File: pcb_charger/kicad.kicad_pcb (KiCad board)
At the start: 2 copper layers, 100 x 30 mm, 12 parts, among them J1 B+, J2 B-, J3 OUT+, J4 OUT-, M1 TP4056Module, SW1 SW_SPDT

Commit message: All 3 parts done
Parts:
- moved J4 0.70 mm to (80.6, 23.0)
- moved J3 0.50 mm to (60.5, 23.0)
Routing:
- net Net-(J3-Pad1): track 41.6 -> 38.9 mm
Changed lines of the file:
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@@
     (thickness 1.6)
     (drawings 91)
-    (tracks 35)
+    (tracks 33)
     (zones 0)
     (modules 12)
@@
     (mod_text_size 1 1)
     (mod_text_width 0.15)
-    (pad_size 15 2.5)
+    (pad_size 15 3)
     (pad_drill 0)
     (pad_to_mask_clearance 0.2)
@@
   )
   (module Connector_Wire:SolderWirePad_1x01_Drill0.8mm (layer B.Cu)
-    (at 80.575 22.3)
+    (at 80.575 23)
     (descr "Wire solder connection")
     (tags connector)
@@
       (effects (font (size 1 1) (thickness 0.15)) (justify mirror))
     )
-    (pad 1 smd oval (at 0 0) (size 15 2.5) (layers B.Cu B.Paste B.Mask)
+    (pad 1 smd oval (at 0 0) (size 15 3) (layers B.Cu B.Paste B.Mask)
       (net 4 "Net-(J4-Pad1)"))
   )
   (module Connector_Wire:SolderWirePad_1x01_Drill0.8mm (layer B.Cu)
-    (at 60.5 22.5)
+    (at 60.5 23)
     (descr "Wire solder connection")
     (tags connector)
@@
       (effects (font (size 1 1) (thickness 0.15)) (justify mirror))
     )
-    (pad 1 smd oval (at 0 0) (size 15 2.5) (layers B.Cu B.Paste B.Mask)
+    (pad 1 smd oval (at 0 0) (size 15 3) (layers B.Cu B.Paste B.Mask)
       (net 3 "Net-(J3-Pad1)"))
   )
@@
   (segment (start 84.25 44.118) (end 84.216 44.084) (width 0.3) (layer F.Cu) (net 3))
   (segment (start 84.25 47.07) (end 84.25 44.118) (width 0.3) (layer F.Cu) (net 3))
-  (segment (start 84.216 44.084) (end 84.216 33.924) (width 0.3) (layer B.Cu) (net 3))
-  (segment (start 84.216 33.924) (end 75.072 24.78) (width 0.3) (layer B.Cu) (net 3))
-  (segment (start 68.3 22.5) (end 60.5 22.5) (width 0.3) (layer B.Cu) (net 3))
-  (segment (start 70.58 24.78) (end 68.3 22.5) (width 0.3) (layer B.Cu) (net 3))
-  (segment (start 75.072 24.78) (end 70.58 24.78) (width 0.3) (layer B.Cu) (net 3))
+  (segment (start 84.216 38.216) (end 84.216 44.084) (width 0.3) (layer B.Cu) (net 3))
+  (segment (start 60.5 23) (end 69 23) (width 0.3) (layer B.Cu) (net 3))
+  (segment (start 69 23) (end 84.216 38.216) (width 0.3) (layer B.Cu) (net 3))
   (segment (start 80.575 23.85) (end 80.575 22.3) (width 0.3) (layer B.Cu) (net 4))
   (segment (start 80.575 28.875) (end 80.575 28.075) (width 0.3) (layer B.Cu) (net 4))

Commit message: Last changes to the charger board and gerbers
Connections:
- net Net-(J1-Pad1) renamed /B+
- net Net-(J2-Pad1) renamed /B-
- net Net-(J3-Pad1) renamed /OUT+on
- net Net-(J4-Pad1) renamed /OUT-
- net Net-(M1-Pad5) renamed /OUT+
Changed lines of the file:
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@@
   )
   (net 0 "")
-  (net 1 "Net-(J1-Pad1)")
-  (net 2 "Net-(J2-Pad1)")
-  (net 3 "Net-(J3-Pad1)")
-  (net 4 "Net-(J4-Pad1)")
-  (net 5 "Net-(M1-Pad5)")
+  (net 1 /B+)
+  (net 2 /B-)
+  (net 3 /OUT+on)
+  (net 4 /OUT-)
+  (net 5 /OUT+)
   (net_class Default "This is the default net class."
     (clearance 0.2)
@@
     (uvia_dia 0.3)
     (uvia_drill 0.1)
-    (add_net "Net-(J1-Pad1)")
-    (add_net "Net-(J2-Pad1)")
-    (add_net "Net-(J3-Pad1)")
-    (add_net "Net-(J4-Pad1)")
-    (add_net "Net-(M1-Pad5)")
+    (add_net /B+)
+    (add_net /B-)
+    (add_net /OUT+)
+    (add_net /OUT+on)
+    (add_net /OUT-)
   )
   (module logos:roommonitor-rev (layer F.Cu)
@@
     (pad 3 smd rect (at 2.25 -1.43) (size 0.7 1.5) (layers F.Cu F.Paste F.Mask))
     (pad 2 smd rect (at 0.75 -1.43) (size 0.7 1.5) (layers F.Cu F.Paste F.Mask)
-      (net 5 "Net-(M1-Pad5)"))
+      (net 5 /OUT+))
     (pad 1 smd rect (at -2.25 -1.43) (size 0.7 1.5) (layers F.Cu F.Paste F.Mask)
-      (net 3 "Net-(J3-Pad1)"))
+      (net 3 /OUT+on))
     (pad "" np_thru_hole circle (at 1.5 0.33) (size 0.9 0.9) (drill 0.9) (layers *.Cu *.Mask))
     (pad "" np_thru_hole circle (at -1.5 0.33) (size 0.9 0.9) (drill 0.9) (layers *.Cu *.Mask))
@@
     (pad 2 smd rect (at -11 -6.75 180) (size 3 3) (layers B.Cu B.Paste B.Mask))
     (pad 6 smd rect (at 11 -7 180) (size 3 2.5) (layers B.Cu B.Paste B.Mask)
-      (net 4 "Net-(J4-Pad1)"))
+      (net 4 /OUT-))
     (pad 5 smd rect (at 11 7 180) (size 3 2.5) (layers B.Cu B.Paste B.Mask)
-      (net 5 "Net-(M1-Pad5)"))
+      (net 5 /OUT+))
     (pad 3 smd rect (at 11 3.75 180) (size 3 2.5) (layers B.Cu B.Paste B.Mask)
-      (net 1 "Net-(J1-Pad1)"))
+      (net 1 /B+))
     (pad 4 smd rect (at 11 -3.75 180) (size 3 2.5) (layers B.Cu B.Paste B.Mask)
-      (net 2 "Net-(J2-Pad1)"))
+      (net 2 /B-))
   )
   (module Connector_Wire:SolderWirePad_1x01_Drill0.8mm (layer B.Cu)
@@
     )
     (pad 1 smd oval (at 0 0) (size 15 3) (layers B.Cu B.Paste B.Mask)
-      (net 4 "Net-(J4-Pad1)"))
+      (net 4 /OUT-))
   )
   (module Connector_Wire:SolderWirePad_1x01_Drill0.8mm (layer B.Cu)
@@
     )
     (pad 1 smd oval (at 0 0) (size 15 3) (layers B.Cu B.Paste B.Mask)
-      (net 3 "Net-(J3-Pad1)"))
+      (net 3 /OUT+on))
   )
   (module Connector_Wire:SolderWirePad_1x01_Drill0.8mm (layer B.Cu)
@@
     )
     (pad 1 smd oval (at 0 0) (size 14 2.5) (layers B.Cu B.Paste B.Mask)
-      (net 2 "Net-(J2-Pad1)"))
+      (net 2 /B-))
   )
   (module Connector_Wire:SolderWirePad_1x01_Drill0.8mm (layer B.Cu)
@@
     )
     (pad 1 smd oval (at 0 0) (size 14 2.5) (layers B.Cu B.Paste B.Mask)
-      (net 1 "Net-(J1-Pad1)"))
+      (net 1 /B+))
   )
   (gr_text OFF (at 93 49) (layer F.SilkS)
@@
   (via (at 92.598 32.908) (size 0.6) (drill 0.4) (layers F.Cu B.Cu) (net 1))
   (segment (start 51.378 24.2) (end 51.45 24.272) (width 0.3) (layer B.Cu) (net 1))
-  (segment (start 42.9 24.2) (end 51.378 24.2) (width 0.3) (layer B.Cu) (net 1))
+  (segment (start 42.9 24.2) (end 51.378 24.2) (width 0.3) (layer B.Cu) (net 1) (status 10))
   (segment (start 92.994001 32.511999) (end 92.598 32.908) (width 0.3) (layer F.Cu) (net 1))
   (segment (start 92.994001 29.547999) (end 92.994001 32.511999) (width 0.3) (layer F.Cu) (net 1))
-  (segment (start 51.45 24.272) (end 87.718002 24.272) (width 0.3) (layer F.Cu) (net 1))
   (segment (start 87.718002 24.272) (end 92.994001 29.547999) (width 0.3) (layer F.Cu) (net 1))
   (segment (start 93.756 31.75) (end 92.598 32.908) (width 0.3) (layer B.Cu) (net 1))
-  (segment (start 96 31.75) (end 93.756 31.75) (width 0.3) (layer B.Cu) (net 1))
+  (segment (start 96 31.75) (end 93.756 31.75) (width 0.3) (layer B.Cu) (net 1) (status 10))
+  (segment (start 51.45 24.272) (end 87.718002 24.272) (width 0.3) (layer F.Cu) (net 1))
   (segment (start 97.85 25.7) (end 102 29.85) (width 0.3) (layer B.Cu) (net 2))
-  (segment (start 97.85 24.15) (end 97.85 25.7) (width 0.3) (layer B.Cu) (net 2))
+  (segment (start 97.85 24.15) (end 97.85 25.7) (width 0.3) (layer B.Cu) (net 2) (status 10))
   (segment (start 102 29.85) (end 102 36) (width 0.3) (layer B.Cu) (net 2))
-  (segment (start 98.75 39.25) (end 96 39.25) (width 0.3) (layer B.Cu) (net 2))
+  (segment (start 98.75 39.25) (end 96 39.25) (width 0.3) (layer B.Cu) (net 2) (status 20))
   (segment (start 102 36) (end 98.75 39.25) (width 0.3) (layer B.Cu) (net 2))
   (via (at 84.216 44.084) (size 0.6) (drill 0.4) (layers F.Cu B.Cu) (net 3))
   (segment (start 84.25 44.118) (end 84.216 44.084) (width 0.3) (layer F.Cu) (net 3))
-  (segment (start 84.25 47.07) (end 84.25 44.118) (width 0.3) (layer F.Cu) (net 3))
+  (segment (start 84.25 47.07) (end 84.25 44.118) (width 0.3) (layer F.Cu) (net 3) (status 10))
   (segment (start 84.216 38.216) (end 84.216 44.084) (width 0.3) (layer B.Cu) (net 3))
-  (segment (start 60.5 23) (end 69 23) (width 0.3) (layer B.Cu) (net 3))
+  (segment (start 60.5 23) (end 69 23) (width 0.3) (layer B.Cu) (net 3) (status 10))
   (segment (start 69 23) (end 84.216 38.216) (width 0.3) (layer B.Cu) (net 3))
-  (segment (start 80.575 23.85) (end 80.575 22.3) (width 0.3) (layer B.Cu) (net 4))
+  (segment (start 80.575 23.85) (end 80.575 22.3) (width 0.3) (layer B.Cu) (net 4) (status 30))
   (segment (start 80.575 28.875) (end 80.575 28.075) (width 0.3) (layer B.Cu) (net 4))
   (segment (start 94.2 42.5) (end 80.575 28.875) (width 0.3) (layer B.Cu) (net 4))
-  (segment (start 96 42.5) (end 94.2 42.5) (width 0.3) (layer B.Cu) (net 4))
+  (segment (start 96 42.5) (end 94.2 42.5) (width 0.3) (layer B.Cu) (net 4) (status 10))
   (segment (start 80.575 28.825) (end 80.575 28.075) (width 0.3) (layer B.Cu) (net 4))
-  (segment (start 80.575 28.075) (end 80.575 23.85) (width 0.3) (layer B.Cu) (net 4))
+  (segment (start 80.575 28.075) (end 80.575 23.85) (width 0.3) (layer B.Cu) (net 4) (status 20))
   (via (at 92.344 29.86) (size 0.6) (drill 0.4) (layers F.Cu B.Cu) (net 5))
   (segment (start 92.484 30) (end 92.344 29.86) (width 0.3) (layer B.Cu) (net 5))
-  (segment (start 87.25 34.954) (end 87.25 47.07) (width 0.3) (layer F.Cu) (net 5))
+  (segment (start 87.25 34.954) (end 87.25 47.07) (width 0.3) (layer F.Cu) (net 5) (status 20))
   (segment (start 92.344 29.86) (end 87.25 34.954) (width 0.3) (layer F.Cu) (net 5))
   (segment (start 93.704 28.5) (end 92.344 29.86) (width 0.3) (layer B.Cu) (net 5))
-  (segment (start 96 28.5) (end 93.704 28.5) (width 0.3) (layer B.Cu) (net 5))
+  (segment (start 96 28.5) (end 93.704 28.5) (width 0.3) (layer B.Cu) (net 5) (status 10))
 )

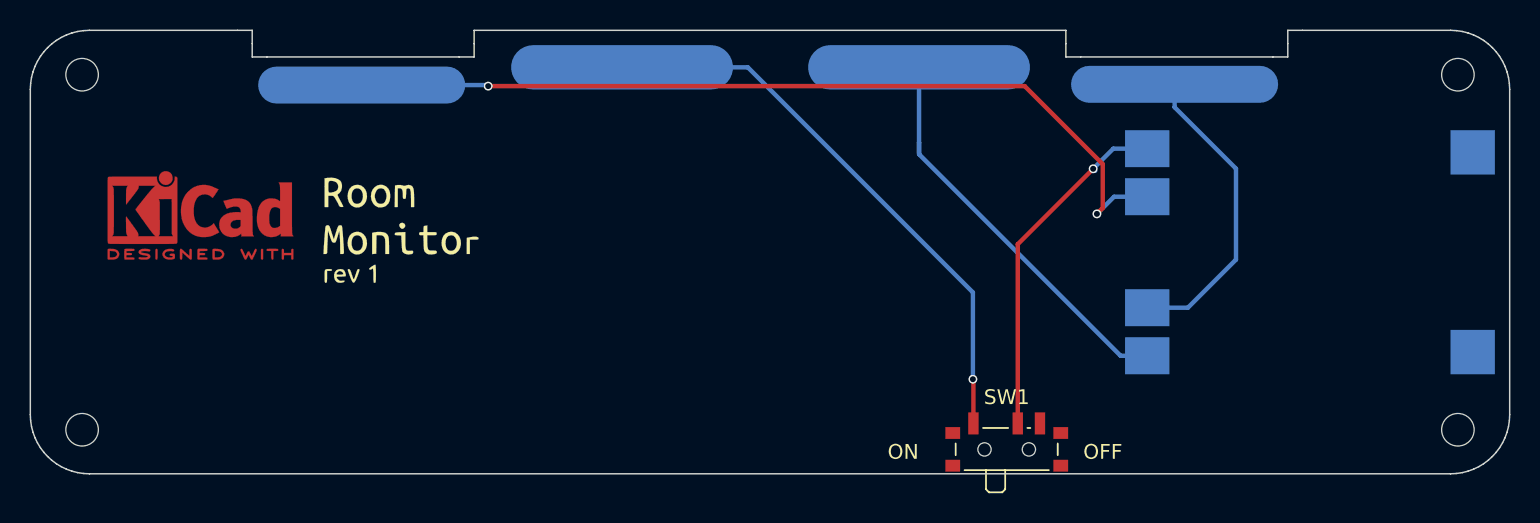
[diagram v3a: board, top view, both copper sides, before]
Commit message: Update trace and via sizes for battery and charger
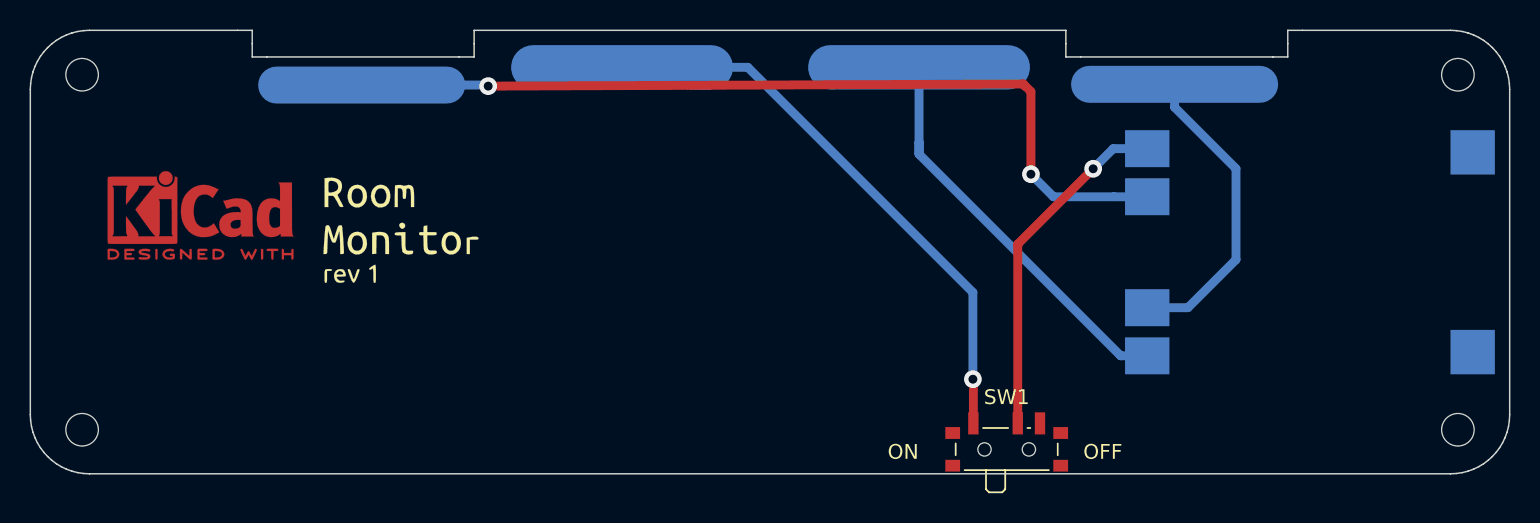
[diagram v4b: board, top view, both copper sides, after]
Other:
- net class Battery added: clearance 0.4, trace_width 0.6, via_dia 1.2, via_drill 0.6
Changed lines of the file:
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@@
-(kicad_pcb (version 20171130) (host pcbnew 5.1.4-e60b266~84~ubuntu19.04.1)
+(kicad_pcb (version 20171130) (host pcbnew 5.1.5-52549c5~84~ubuntu19.04.1)
   (general
     (thickness 1.6)
     (drawings 91)
-    (tracks 33)
+    (tracks 36)
     (zones 0)
     (modules 12)
@@
     (via_dia 0.6)
     (via_drill 0.4)
+    (uvia_dia 0.3)
+    (uvia_drill 0.1)
+  )
+  (net_class Battery ""
+    (clearance 0.4)
+    (trace_width 0.6)
+    (via_dia 1.2)
+    (via_drill 0.6)
     (uvia_dia 0.3)
     (uvia_drill 0.1)
@@
   (gr_line (start 116.499999 50.477394) (end 116.499999 50.477394) (layer Edge.Cuts) (width 0.1))
   (gr_line (start 116.499999 50.477394) (end 116.499999 50.477394) (layer Edge.Cuts) (width 0.1))
-  (via (at 51.45 24.272) (size 0.6) (drill 0.4) (layers F.Cu B.Cu) (net 1))
-  (via (at 92.598 32.908) (size 0.6) (drill 0.4) (layers F.Cu B.Cu) (net 1))
-  (segment (start 51.378 24.2) (end 51.45 24.272) (width 0.3) (layer B.Cu) (net 1))
-  (segment (start 42.9 24.2) (end 51.378 24.2) (width 0.3) (layer B.Cu) (net 1) (status 10))
-  (segment (start 92.994001 32.511999) (end 92.598 32.908) (width 0.3) (layer F.Cu) (net 1))
-  (segment (start 92.994001 29.547999) (end 92.994001 32.511999) (width 0.3) (layer F.Cu) (net 1))
-  (segment (start 87.718002 24.272) (end 92.994001 29.547999) (width 0.3) (layer F.Cu) (net 1))
-  (segment (start 93.756 31.75) (end 92.598 32.908) (width 0.3) (layer B.Cu) (net 1))
-  (segment (start 96 31.75) (end 93.756 31.75) (width 0.3) (layer B.Cu) (net 1) (status 10))
-  (segment (start 51.45 24.272) (end 87.718002 24.272) (width 0.3) (layer F.Cu) (net 1))
-  (segment (start 97.85 25.7) (end 102 29.85) (width 0.3) (layer B.Cu) (net 2))
-  (segment (start 97.85 24.15) (end 97.85 25.7) (width 0.3) (layer B.Cu) (net 2) (status 10))
-  (segment (start 102 29.85) (end 102 36) (width 0.3) (layer B.Cu) (net 2))
-  (segment (start 98.75 39.25) (end 96 39.25) (width 0.3) (layer B.Cu) (net 2) (status 20))
-  (segment (start 102 36) (end 98.75 39.25) (width 0.3) (layer B.Cu) (net 2))
-  (via (at 84.216 44.084) (size 0.6) (drill 0.4) (layers F.Cu B.Cu) (net 3))
-  (segment (start 84.25 44.118) (end 84.216 44.084) (width 0.3) (layer F.Cu) (net 3))
-  (segment (start 84.25 47.07) (end 84.25 44.118) (width 0.3) (layer F.Cu) (net 3) (status 10))
-  (segment (start 84.216 38.216) (end 84.216 44.084) (width 0.3) (layer B.Cu) (net 3))
-  (segment (start 60.5 23) (end 69 23) (width 0.3) (layer B.Cu) (net 3) (status 10))
-  (segment (start 69 23) (end 84.216 38.216) (width 0.3) (layer B.Cu) (net 3))
-  (segment (start 80.575 23.85) (end 80.575 22.3) (width 0.3) (layer B.Cu) (net 4) (status 30))
-  (segment (start 80.575 28.875) (end 80.575 28.075) (width 0.3) (layer B.Cu) (net 4))
-  (segment (start 94.2 42.5) (end 80.575 28.875) (width 0.3) (layer B.Cu) (net 4))
-  (segment (start 96 42.5) (end 94.2 42.5) (width 0.3) (layer B.Cu) (net 4) (status 10))
-  (segment (start 80.575 28.825) (end 80.575 28.075) (width 0.3) (layer B.Cu) (net 4))
-  (segment (start 80.575 28.075) (end 80.575 23.85) (width 0.3) (layer B.Cu) (net 4) (status 20))
-  (via (at 92.344 29.86) (size 0.6) (drill 0.4) (layers F.Cu B.Cu) (net 5))
-  (segment (start 92.484 30) (end 92.344 29.86) (width 0.3) (layer B.Cu) (net 5))
-  (segment (start 87.25 34.954) (end 87.25 47.07) (width 0.3) (layer F.Cu) (net 5) (status 20))
-  (segment (start 92.344 29.86) (end 87.25 34.954) (width 0.3) (layer F.Cu) (net 5))
-  (segment (start 93.704 28.5) (end 92.344 29.86) (width 0.3) (layer B.Cu) (net 5))
-  (segment (start 96 28.5) (end 93.704 28.5) (width 0.3) (layer B.Cu) (net 5) (status 10))
+  (via (at 51.45 24.272) (size 1.2) (drill 0.6) (layers F.Cu B.Cu) (net 1))
+  (segment (start 51.378 24.2) (end 51.45 24.272) (width 0.6) (layer B.Cu) (net 1))
+  (segment (start 42.9 24.2) (end 51.378 24.2) (width 0.6) (layer B.Cu) (net 1) (status 10))
+  (segment (start 96 31.75) (end 93.756 31.75) (width 0.6) (layer B.Cu) (net 1) (status 10))
+  (segment (start 93.756 31.75) (end 89.662 31.75) (width 0.6) (layer B.Cu) (net 1))
+  (segment (start 89.662 31.75) (end 88.138 30.226) (width 0.6) (layer B.Cu) (net 1))
+  (segment (start 88.138 30.226) (end 88.138 30.226) (width 0.6) (layer B.Cu) (net 1))
+  (via (at 88.138 30.226) (size 1.2) (drill 0.6) (layers F.Cu B.Cu) (net 1))
+  (segment (start 88.138 24.638) (end 87.63 24.13) (width 0.6) (layer F.Cu) (net 1))
+  (segment (start 88.138 30.226) (end 88.138 24.638) (width 0.6) (layer F.Cu) (net 1))
+  (segment (start 51.45 24.272) (end 87.63 24.13) (width 0.6) (layer F.Cu) (net 1))
+  (segment (start 87.63 24.13) (end 87.718002 24.272) (width 0.6) (layer F.Cu) (net 1))
+  (segment (start 97.85 25.7) (end 102 29.85) (width 0.6) (layer B.Cu) (net 2))
+  (segment (start 97.85 24.15) (end 97.85 25.7) (width 0.6) (layer B.Cu) (net 2) (status 10))
+  (segment (start 102 29.85) (end 102 36) (width 0.6) (layer B.Cu) (net 2))
+  (segment (start 98.75 39.25) (end 96 39.25) (width 0.6) (layer B.Cu) (net 2) (status 20))
+  (segment (start 102 36) (end 98.75 39.25) (width 0.6) (layer B.Cu) (net 2))
+  (via (at 84.216 44.084) (size 1.2) (drill 0.6) (layers F.Cu B.Cu) (net 3))
+  (segment (start 84.25 44.118) (end 84.216 44.084) (width 0.6) (layer F.Cu) (net 3))
+  (segment (start 84.25 47.07) (end 84.25 44.118) (width 0.6) (layer F.Cu) (net 3) (status 10))
+  (segment (start 84.216 38.216) (end 84.216 44.084) (width 0.6) (layer B.Cu) (net 3))
+  (segment (start 60.5 23) (end 69 23) (width 0.6) (layer B.Cu) (net 3) (status 10))
+  (segment (start 69 23) (end 84.216 38.216) (width 0.6) (layer B.Cu) (net 3))
+  (segment (start 80.575 23.85) (end 80.575 22.3) (width 0.6) (layer B.Cu) (net 4) (status 30))
+  (segment (start 80.575 28.875) (end 80.575 28.075) (width 0.6) (layer B.Cu) (net 4))
+  (segment (start 94.2 42.5) (end 80.575 28.875) (width 0.6) (layer B.Cu) (net 4))
+  (segment (start 96 42.5) (end 94.2 42.5) (width 0.6) (layer B.Cu) (net 4) (status 10))
+  (segment (start 80.575 28.825) (end 80.575 28.075) (width 0.6) (layer B.Cu) (net 4))
+  (segment (start 80.575 28.075) (end 80.575 23.85) (width 0.6) (layer B.Cu) (net 4) (status 20))
+  (segment (start 92.344 29.86) (end 92.344 29.86) (width 0.6) (layer B.Cu) (net 5))
+  (segment (start 96 28.5) (end 93.704 28.5) (width 0.6) (layer B.Cu) (net 5) (status 10))
+  (segment (start 92.344 29.86) (end 92.344 29.86) (width 0.6) (layer F.Cu) (net 5))
+  (segment (start 87.25 34.954) (end 87.25 47.07) (width 0.6) (layer F.Cu) (net 5) (status 20))
+  (segment (start 93.704 28.5) (end 92.344 29.86) (width 0.6) (layer B.Cu) (net 5))
+  (segment (start 92.344 29.86) (end 87.25 34.954) (width 0.6) (layer F.Cu) (net 5))
+  (via (at 92.344 29.86) (size 1.2) (drill 0.6) (layers F.Cu B.Cu) (net 5))
 )
